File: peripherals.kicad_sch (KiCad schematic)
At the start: 0 parts

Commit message: Add power sheet and update schematic connections
Added a new power sheet to the project and updated the main schematic to include connections for power, MCU, peripherals, and Ethernet PHY. Also added backup files and updated the Ethernet PHY schematic with symbol definitions and pin mappings.
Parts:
- added C2: 0.1 uF, symbol Device:C
- added C26, C27, C29, C31: 0.01uF, symbol Device:C
- added C28, C30: 1000pF, symbol Device:C
- added C32, C33, C34, C35: 0.1uF, symbol Device:C
- added J1: RJ45_Shielded, symbol MyLibrary:RJ45_Shielded
- added J2: Conn_ARM_JTAG_SWD_10, Connector_PinHeader_1.27mm:PinHeader_2x05_P1.27mm_Vertical, symbol Connector:Conn_ARM_JTAG_SWD_10
- added JP2: Jumper_2_Open, symbol Jumper:Jumper_2_Open
- added R10, R11, R8, R9: 75, symbol Device:R
- added S1: SKRPABE010, SKRPABE010:SW_SKRPABE010, symbol SKRPABE010:SKRPABE010
- added T1: WE-LAN_749013011A, WE-LAN_749013011A:WE-LAN_749013011A, symbol WE-LAN_749013011A:WE-LAN_749013011A
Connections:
- new net: C28.1, R8.2, R9.2
- new net: C27.1, J1.4, J1.5
- new net: C27.2, R9.1
- new net: C29.2, R10.1
- new net: C30.1, R10.2, R11.2
- new net: C32.1, C33.1, T1.10 (CRX)
- new net: J1.1, T1.1 (TD+)
- new net: J1.2, T1.3 (TD-)
- new net: J1.3, T1.6 (RD+)
- new net: J1.6, T1.8 (RD-)
- new net: C26.1, J1.7, J1.8
- new net: C31.2, R11.1
- new net: C26.2, R8.1
- new net: C34.1, C35.1, T1.15 (CTX)
- new net +3V3: J2.1 (VTref)
- new net +48V: C29.1, T1.2 (CTD)
- new net -48V: C31.1, T1.7 (CRD)
- new net ETH_RD_M: T1.9 (RX-)
- new net ETH_RD_P: T1.11 (RX+)
- new net ETH_TD_M: T1.14 (TX-)
- new net ETH_TD_P: T1.16 (TX+)
- new net Earth: C28.2, C30.2, J1.SH
- new net GND: C2.2, C32.2, C33.2, C34.2, C35.2, J2.3 (GND), J2.5 (GND), JP2.2 (B), S1.3, S1.4
- new net GND Detect: J2.9 (GNDDetect), JP2.1 (A)
- new net MCU_RST: J2.10 (~{RESET})
- new net RST: C2.1, S1.1, S1.2
- new net SWCLK: J2.4 (SWCLK/TCK)
- new net SWDIO: J2.2 (SWDIO/TMS)
- no-connect marks 0 -> 2

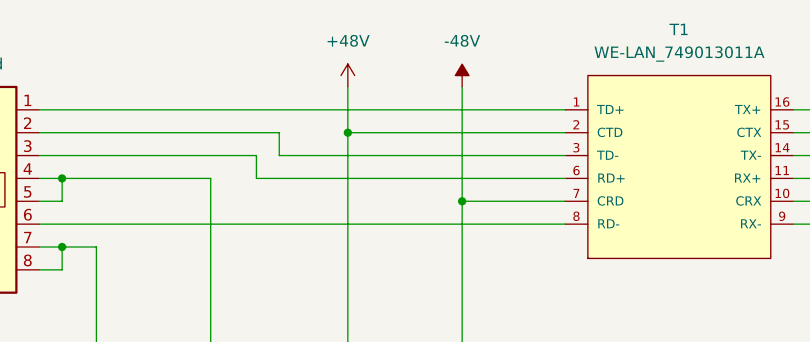
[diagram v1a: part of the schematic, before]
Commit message: Update schematic power symbols and add backups
Replaced +48V and -48V power symbols with VDD and VSS in peripherals.kicad_sch, updated title blocks and paper sizes in all .kicad_sch files, and added new schematic symbols for test points, capacitors, resistors, MOSFET, and optocoupler in power.kicad_sch. Added multiple new backup ZIP files for POETempSensor.
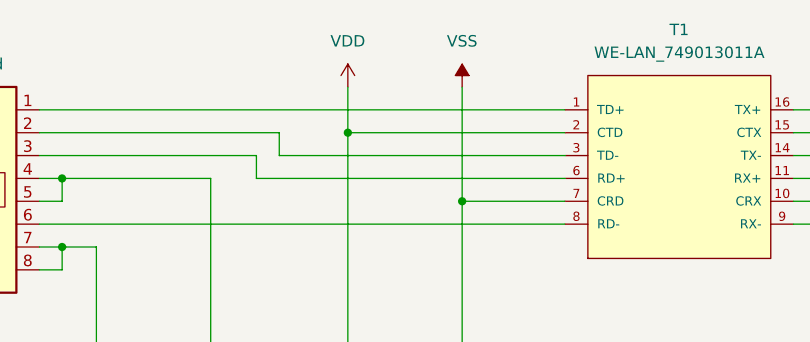
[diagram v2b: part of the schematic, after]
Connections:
- net +48V renamed VDD
- net -48V renamed VSS
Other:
- title: (none) -> Peripherals
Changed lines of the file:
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@@
 	(generator_version "9.0")
 	(paper "A4")
+	(title_block
+		(title "Peripherals")
+		(date "2025-11-09")
+		(rev "v0.1")
+	)
 	(junction
 		(at 146.05 63.5)
@@
 	)
 	(symbol
-		(lib_id "power:+48V")
-		(at 80.01 26.67 0)
-		(unit 1)
-		(exclude_from_sim no)
-		(in_bom yes)
-		(on_board yes)
-		(dnp no)
-		(fields_autoplaced yes)
-		(property "Reference" "#PWR032"
-			(at 80.01 30.48 0)
-			(effects
-				(font
-					(size 1.27 1.27)
-				)
-				(hide yes)
-			)
-		)
-		(property "Value" "+48V"
-			(at 80.01 21.59 0)
-			(effects
-				(font
-					(size 1.27 1.27)
-				)
-			)
-		)
-		(property "Footprint" ""
-			(at 80.01 26.67 0)
-			(effects
-				(font
-					(size 1.27 1.27)
-				)
-				(hide yes)
-			)
-		)
-		(property "Datasheet" ""
-			(at 80.01 26.67 0)
-			(effects
-				(font
-					(size 1.27 1.27)
-				)
-				(hide yes)
-			)
-		)
-		(property "Description" "Power symbol creates a global label with name \"+48V\""
-			(at 80.01 26.67 0)
-			(effects
-				(font
-					(size 1.27 1.27)
-				)
-				(hide yes)
-			)
-		)
-		(pin "1"
-		)
-		(instances
-			(project ""
-				(path "/8882cb81-f0f1-4079-b773-46d85e112905/3cd4941e-3cef-4c26-81e6-dd9cbafa0324"
-					(reference "#PWR032")
-					(unit 1)
-				)
-			)
-		)
-	)
-	(symbol
 		(lib_id "Device:C")
 		(at 134.62 57.15 0)
@@
 	)
 	(symbol
-		(lib_id "power:-48V")
-		(at 92.71 26.67 0)
-		(unit 1)
-		(exclude_from_sim no)
-		(in_bom yes)
-		(on_board yes)
-		(dnp no)
-		(fields_autoplaced yes)
-		(property "Reference" "#PWR033"
-			(at 92.71 30.48 0)
-			(effects
-				(font
-					(size 1.27 1.27)
-				)
-				(hide yes)
-			)
-		)
-		(property "Value" "-48V"
-			(at 92.71 21.59 0)
-			(effects
-				(font
-					(size 1.27 1.27)
-				)
-			)
-		)
-		(property "Footprint" ""
-			(at 92.71 26.67 0)
-			(effects
-				(font
-					(size 1.27 1.27)
-				)
-				(hide yes)
-			)
-		)
-		(property "Datasheet" ""
-			(at 92.71 26.67 0)
-			(effects
-				(font
-					(size 1.27 1.27)
-				)
-				(hide yes)
-			)
-		)
-		(property "Description" "Power symbol creates a global label with name \"-48V\""
-			(at 92.71 26.67 0)
-			(effects
-				(font
-					(size 1.27 1.27)
-				)
-				(hide yes)
-			)
-		)
-		(pin "1"
-		)
-		(instances
-			(project ""
-				(path "/8882cb81-f0f1-4079-b773-46d85e112905/3cd4941e-3cef-4c26-81e6-dd9cbafa0324"
-					(reference "#PWR033")
-					(unit 1)
-				)
-			)
-		)
-	)
-	(symbol
 		(lib_id "MyLibrary:RJ45_Shielded")
 		(at 35.56 38.1 0)
@@
 	)
 	(symbol
+		(lib_id "power:VSS")
+		(at 92.71 26.67 0)
+		(unit 1)
+		(exclude_from_sim no)
+		(in_bom yes)
+		(on_board yes)
+		(dnp no)
+		(fields_autoplaced yes)
+		(property "Reference" "#PWR043"
+			(at 92.71 30.48 0)
+			(effects
+				(font
+					(size 1.27 1.27)
+				)
+				(hide yes)
+			)
+		)
+		(property "Value" "VSS"
+			(at 92.71 21.59 0)
+			(effects
+				(font
+					(size 1.27 1.27)
+				)
+			)
+		)
+		(property "Footprint" ""
+			(at 92.71 26.67 0)
+			(effects
+				(font
+					(size 1.27 1.27)
+				)
+				(hide yes)
+			)
+		)
+		(property "Datasheet" ""
+			(at 92.71 26.67 0)
+			(effects
+				(font
+					(size 1.27 1.27)
+				)
+				(hide yes)
+			)
+		)
+		(property "Description" "Power symbol creates a global label with name \"VSS\""
+			(at 92.71 26.67 0)
+			(effects
+				(font
+					(size 1.27 1.27)
+				)
+				(hide yes)
+			)
+		)
+		(pin "1"
+		)
+		(instances
+			(project ""
+				(path "/8882cb81-f0f1-4079-b773-46d85e112905/3cd4941e-3cef-4c26-81e6-dd9cbafa0324"
+					(reference "#PWR043")
+					(unit 1)
+				)
+			)
+		)
+	)
+	(symbol
 		(lib_id "power:GND")
 		(at 260.35 45.72 0)
@@
 					(unit 1)
 				)
+			)
+		)
+	)
+	(symbol
+		(lib_id "power:VDD")
+		(at 80.01 26.67 0)
+		(unit 1)
+		(exclude_from_sim no)
+		(in_bom yes)
+		(on_board yes)
+		(dnp no)
+		(fields_autoplaced yes)
+		(property "Reference" "#PWR032"
+			(at 80.01 30.48 0)
+			(effects
+				(font
+					(size 1.27 1.27)
+				)
+				(hide yes)
+			)
+		)
+		(property "Value" "VDD"
+			(at 80.01 21.59 0)
+			(effects
+				(font
+					(size 1.27 1.27)
+				)
+			)
+		)
+		(property "Footprint" ""
+			(at 80.01 26.67 0)
+			(effects
+				(font
+					(size 1.27 1.27)
+				)
+				(hide yes)
+			)
+		)
+		(property "Datasheet" ""
+			(at 80.01 26.67 0)
+			(effects
+				(font
+					(size 1.27 1.27)
+				)
+				(hide yes)
+			)
+		)
+		(property "Description" "Power symbol creates a global label with name \"VDD\""
+			(at 80.01 26.67 0)
+			(effects
+				(font
+					(size 1.27 1.27)
+				)
+				(hide yes)
+			)
+		)
+		(pin "1"
+		)
+		(instances
+			(project ""
+				(path "/8882cb81-f0f1-4079-b773-46d85e112905/3cd4941e-3cef-4c26-81e6-dd9cbafa0324"
+					(reference "#PWR032")
+					(unit 1)
+				)
